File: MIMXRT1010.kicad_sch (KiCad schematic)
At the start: 28 parts, among them J1 Conn_01x02, U1 MIMXRT1011DAE5A, Y1 32.68KHz, Y2 24 MHZ

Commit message: anjir
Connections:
- net LPUART3_RXD_ALT0: now reaches U1.1 (GPIO_11)
- net LPUART4_TXD_ALT0: now reaches U1.58 (GPIO_AD_02)
- net LPUART4_RXD_ALT0: now reaches U1.59 (GPIO_AD_01)
- net LPUART1_TXD_ALT2: now reaches U1.62 (GPIO_SD_12)
- net LPUART1_RXD_ALT2: now reaches U1.64 (GPIO_SD_11)
- net LPUART2_TXD_ALT2: now reaches U1.65 (GPIO_SD_10)
- net LPUART2_RXD_ALT2: now reaches U1.66 (GPIO_SD_09)
- net LPUART3_TXD_ALT0: now reaches U1.80 (GPIO_12)
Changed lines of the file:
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@@
+	(wire
+		(pts
+			(xy 212.09 41.91) (xy 245.11 41.91)
+		)
+		(stroke
+			(width 0)
+			(type default)
+		)
+	)
 	(wire
 		(pts
@@
 	(wire
 		(pts
-			(xy 212.09 133.35) (xy 224.79 133.35)
+			(xy 212.09 133.35) (xy 241.3 133.35)
 		)
 		(stroke
@@
 	(wire
 		(pts
+			(xy 212.09 95.25) (xy 234.95 95.25)
+		)
+		(stroke
+			(width 0)
+			(type default)
+		)
+	)
+	(wire
+		(pts
 			(xy 20.32 118.11) (xy 20.32 129.54)
 		)
@@
 	(wire
 		(pts
+			(xy 212.09 80.01) (xy 237.49 80.01)
+		)
+		(stroke
+			(width 0)
+			(type default)
+		)
+	)
+	(wire
+		(pts
 			(xy 247.65 138.43) (xy 252.73 138.43)
 		)
@@
 	(wire
 		(pts
+			(xy 212.09 77.47) (xy 237.49 77.47)
+		)
+		(stroke
+			(width 0)
+			(type default)
+		)
+	)
+	(wire
+		(pts
 			(xy 99.06 158.75) (xy 99.06 157.48)
 		)
@@
 	(wire
 		(pts
+			(xy 58.42 41.91) (xy 85.09 41.91)
+		)
+		(stroke
+			(width 0)
+			(type default)
+		)
+	)
+	(wire
+		(pts
 			(xy 21.59 78.74) (xy 50.8 78.74)
 		)
@@
 	(wire
 		(pts
+			(xy 212.09 97.79) (xy 234.95 97.79)
+		)
+		(stroke
+			(width 0)
+			(type default)
+		)
+	)
+	(wire
+		(pts
 			(xy 85.09 135.89) (xy 69.85 135.89)
 		)
@@
 	(wire
 		(pts
+			(xy 212.09 87.63) (xy 237.49 87.63)
+		)
+		(stroke
+			(width 0)
+			(type default)
+		)
+	)
+	(wire
+		(pts
 			(xy 16.51 106.68) (xy 16.51 105.41)
 		)
@@
 	(wire
 		(pts
+			(xy 212.09 82.55) (xy 237.49 82.55)
+		)
+		(stroke
+			(width 0)
+			(type default)
+		)
+	)
+	(wire
+		(pts
 			(xy 74.93 115.57) (xy 85.09 115.57)
 		)
@@
 	(wire
 		(pts
-			(xy 212.09 130.81) (xy 224.79 130.81)
+			(xy 212.09 130.81) (xy 241.3 130.81)
 		)
 		(stroke
@@
 			(width 0)
 			(type default)
+		)
+	)
+	(text_box "LPUART3 => GNSS\nLPUART1/2 => WIFI\nLPUART4 => PRINTER (KAYAKNYA)\n\nCOMCONFIGURASI LEWAT APA NJIR?"
+		(exclude_from_sim no)
+		(at 17.78 20.32 0)
+		(size 33.02 17.78)
+		(stroke
+			(width 0)
+			(type default)
+		)
+		(fill
+			(type none)
+		)
+		(effects
+			(font
+				(size 1.27 1.27)
+			)
+			(justify left top)
 		)
 	)
@@
 		)
 	)
+	(label "LPUART4_RXD_ALT0"
+		(at 234.95 95.25 180)
+		(fields_autoplaced yes)
+		(effects
+			(font
+				(size 1.27 1.27)
+			)
+			(justify right bottom)
+		)
+	)
 	(label "LPSPI1_SDI"
 		(at 227.33 100.33 180)
@@
 	)
 	(label "JTAG_TCK"
-		(at 224.79 130.81 180)
+		(at 241.3 130.81 180)
 		(fields_autoplaced yes)
 		(effects
@@
 		)
 	)
+	(label "LPUART3_TXD_ALT0"
+		(at 245.11 41.91 180)
+		(fields_autoplaced yes)
+		(effects
+			(font
+				(size 1.27 1.27)
+			)
+			(justify right bottom)
+		)
+	)
+	(label "LPUART2_RXD_ALT2"
+		(at 237.49 77.47 180)
+		(fields_autoplaced yes)
+		(effects
+			(font
+				(size 1.27 1.27)
+			)
+			(justify right bottom)
+		)
+	)
 	(label "OTG1_DN"
 		(at 73.66 120.65 0)
@@
 		)
 	)
+	(label "LPUART3_RXD_ALT0"
+		(at 58.42 41.91 0)
+		(fields_autoplaced yes)
+		(effects
+			(font
+				(size 1.27 1.27)
+			)
+			(justify left bottom)
+		)
+	)
 	(label "JTAG_TDO"
 		(at 224.79 123.19 180)
@@
 		)
 	)
+	(label "LPUART4_TXD_ALT0"
+		(at 234.95 97.79 180)
+		(fields_autoplaced yes)
+		(effects
+			(font
+				(size 1.27 1.27)
+			)
+			(justify right bottom)
+		)
+	)
 	(label "JTAG_TMS"
-		(at 224.79 133.35 180)
-		(fields_autoplaced yes)
-		(effects
+		(at 241.3 133.35 180)
+		(fields_autoplaced yes)
+		(effects
+			(font
+				(size 1.27 1.27)
+			)
+			(justify right bottom)
+		)
+	)
+	(label "LPUART1_TXD_ALT2"
+		(at 237.49 87.63 180)
+		(fields_autoplaced yes)
+		(effects
+			(font
+				(size 1.27 1.27)
+			)
+			(justify right bottom)
+		)
+	)
+	(label "LPUART2_TXD_ALT2"
+		(at 237.49 80.01 180)
+		(fields_autoplaced yes)
+		(effects
+			(font
+				(size 1.27 1.27)
+			)
+			(justify right bottom)
+		)
+	)
+	(label "LPUART1_RXD_ALT2"
+		(at 237.49 82.55 180)
+		(fields_autoplaced yes)
+		(effects

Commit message: yara me kya karun
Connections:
- net GPIO_03_ALT2: now reaches U1.10 (GPIO_03)
- net C1_KEYPAD: now reaches U1.67 (GPIO_SD_08)
- net C2_KEYPAD: now reaches U1.68 (GPIO_SD_07)
- net C3_KEYPAD: now reaches U1.69 (GPIO_SD_06)
- net C4_KEYPAD: now reaches U1.70 (GPIO_SD_05)
- net R1_KEYPAD: now reaches U1.72 (GPIO_SD_04)
- net R2_KEYPAD: now reaches U1.73 (GPIO_SD_03)
- net R3_KEYPAD: now reaches U1.74 (GPIO_SD_02)
- net R4_KEYPAD: now reaches U1.75 (GPIO_SD_01)
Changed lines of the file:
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@@
+	(wire
+		(pts
+			(xy 212.09 74.93) (xy 218.44 74.93)
+		)
+		(stroke
+			(width 0)
+			(type default)
+		)
+	)
 	(wire
 		(pts
@@
 	(wire
 		(pts
+			(xy 212.09 62.23) (xy 220.98 62.23)
+		)
+		(stroke
+			(width 0)
+			(type default)
+		)
+	)
+	(wire
+		(pts
 			(xy 224.79 151.13) (xy 236.22 151.13)
 		)
@@
 	(wire
 		(pts
+			(xy 212.09 59.69) (xy 220.98 59.69)
+		)
+		(stroke
+			(width 0)
+			(type default)
+		)
+	)
+	(wire
+		(pts
 			(xy 48.26 158.75) (xy 48.26 160.02)
 		)
@@
 	(wire
 		(pts
+			(xy 212.09 57.15) (xy 220.98 57.15)
+		)
+		(stroke
+			(width 0)
+			(type default)
+		)
+	)
+	(wire
+		(pts
 			(xy 85.09 135.89) (xy 69.85 135.89)
 		)
@@
 	(wire
 		(pts
+			(xy 212.09 67.31) (xy 218.44 67.31)
+		)
+		(stroke
+			(width 0)
+			(type default)
+		)
+	)
+	(wire
+		(pts
 			(xy 16.51 114.3) (xy 16.51 115.57)
 		)
@@
 	(wire
 		(pts
+			(xy 212.09 72.39) (xy 218.44 72.39)
+		)
+		(stroke
+			(width 0)
+			(type default)
+		)
+	)
+	(wire
+		(pts
 			(xy 212.09 102.87) (xy 227.33 102.87)
 		)
@@
 	(wire
 		(pts
+			(xy 49.53 64.77) (xy 85.09 64.77)
+		)
+		(stroke
+			(width 0)
+			(type default)
+		)
+	)
+	(wire
+		(pts
 			(xy 224.79 148.59) (xy 224.79 151.13)
 		)
@@
 	(wire
 		(pts
+			(xy 212.09 54.61) (xy 220.98 54.61)
+		)
+		(stroke
+			(width 0)
+			(type default)
+		)
+	)
+	(wire
+		(pts
 			(xy 48.26 110.49) (xy 48.26 114.3)
+		)
+		(stroke
+			(width 0)
+			(type default)
+		)
+	)
+	(wire
+		(pts
+			(xy 212.09 69.85) (xy 218.44 69.85)
 		)
 		(stroke
@@
 		)
 	)
+	(label "MCU_PWM_CERVO"
+		(at 49.53 64.77 180)
+		(fields_autoplaced yes)
+		(effects
+			(font
+				(size 1.27 1.27)
+			)
+			(justify right bottom)
+		)
+	)
+	(label "C2_KEYPAD"
+		(at 218.44 72.39 0)
+		(fields_autoplaced yes)
+		(effects
+			(font
+				(size 1.27 1.27)
+			)
+			(justify left bottom)
+		)
+	)
+	(label "C1_KEYPAD"
+		(at 218.44 74.93 0)
+		(fields_autoplaced yes)
+		(effects
+			(font
+				(size 1.27 1.27)
+			)
+			(justify left bottom)
+		)
+	)
 	(label "LPSPI1_SCK"
 		(at 227.33 113.03 180)
@@
 		)
 	)
+	(label "C4_KEYPAD"
+		(at 218.44 67.31 0)
+		(fields_autoplaced yes)
+		(effects
+			(font
+				(size 1.27 1.27)
+			)
+			(justify left bottom)
+		)
+	)
 	(label "LPUART4_RXD_ALT0"
 		(at 234.95 95.25 180)
@@
 		)
 	)
+	(label "GPIO_03_ALT2"
+		(at 58.42 64.77 0)
+		(fields_autoplaced yes)
+		(effects
+			(font
+				(size 1.27 1.27)
+			)
+			(justify left bottom)
+		)
+	)
 	(label "5V_USB_OTG"
 		(at 21.59 78.74 0)
@@
 		)
 	)
+	(label "R1_KEYPAD"
+		(at 220.98 62.23 0)
+		(fields_autoplaced yes)
+		(effects
+			(font
+				(size 1.27 1.27)
+			)
+			(justify left bottom)
+		)
+	)
 	(label "DCDC_3V3"
 		(at 262.89 52.07 0)
@@
 		)
 	)
+	(label "C3_KEYPAD"
+		(at 218.44 69.85 0)
+		(fields_autoplaced yes)
+		(effects
+			(font
+				(size 1.27 1.27)
+			)
+			(justify left bottom)
+		)
+	)
 	(label "OTG1_DP"
 		(at 73.66 123.19 0)
@@
 		)
 	)
+	(label "R3_KEYPAD"
+		(at 220.98 57.15 0)
+		(fields_autoplaced yes)
+		(effects
+			(font
+				(size 1.27 1.27)
+			)
+			(justify left bottom)
+		)
+	)
 	(label "LPUART3_TXD_ALT0"
 		(at 245.11 41.91 180)
@@
 		)
 	)
+	(label "R2_KEYPAD"
+		(at 220.98 59.69 0)
+		(fields_autoplaced yes)
+		(effects
+			(font
+				(size 1.27 1.27)
+			)
+			(justify left bottom)
+		)
+	)
 	(label "JTAG_TMS"
 		(at 241.3 133.35 180)
@@
 		)
 	)
+	(label "R4_KEYPAD"
+		(at 220.98 54.61 0)
+		(fields_autoplaced yes)
+		(effects
+			(font
+				(size 1.27 1.27)
+			)
+			(justify left bottom)
+		)
+	)

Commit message: sebelum pemeriksaan terkahir
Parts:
- removed C18: 1.0UF, symbol Device:C_Polarized_US
- removed C19: 0.22UF, symbol Device:C_Polarized_US
- removed J1: Conn_01x02, symbol Connector_Generic:Conn_01x02
- removed R6: DNP, symbol Device:R_US
- added L5: 4.7uH, symbol Device:L
- added R58: 0, symbol Device:R_US
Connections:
- net C1_KEYPAD: now also U1.46 (GPIO_AD_11); no longer U1.67 (GPIO_SD_08)
- net C2_KEYPAD: now also U1.11 (GPIO_02); no longer U1.68 (GPIO_SD_07)
- net C3_KEYPAD: now also U1.12 (GPIO_01); no longer U1.69 (GPIO_SD_06)
- net C4_KEYPAD: now also U1.60 (GPIO_AD_00); no longer U1.70 (GPIO_SD_05)
- net GND: now also U1.34 (NGND_KEL0), R58.1
- net R3_KEYPAD: now also U1.9 (GPIO_04); no longer U1.74 (GPIO_SD_02)
- net R4_KEYPAD: now also U1.79 (GPIO_13); no longer U1.75 (GPIO_SD_01)
- net VDDA_ADC_3P3_MCU: now reaches U1.42
- net GPIO_00: now reaches U1.13 (GPIO_00)
- net VDD_SOC_IN: now reaches U1.14
- net VDD_SOC_IN: now also U1.53 (VDD_SOC_IN), U1.77 (VDD_SOC_IN)
- net DCDC_PSWITCH_MCU: now reaches U1.15 (DCDC_PSWITCH)
- net MCU_DCDC_IN: now reaches U1.17 (DCDC_IN_Q)
- net MCU_DCDC_IN: now also U1.18 (DCDC_IN)
- net at U1.19 (DCDC_LP): now also L5.2
- net LPI2C2_SCL: now reaches U1.2 (GPIO_10)
- net ONOFF: now reaches U1.21 (ONOFF)
- net POR_B: now reaches U1.22 (POR_B)
- net at U1.23 (TEST_MODE): now also R58.2
- net PMIC_ON_REQ: now reaches U1.24 (PMIC_ON_REQ)
- net VDD_SNVS_IN: now reaches U1.25 (VDD_SNVS_IN)
- net LPI2C2_SDA: now reaches U1.3 (GPIO_09)
- net VDDA_2P5_CAP: now reaches U1.35 (VDD_HIGH_CAP)
- net VDD_HIGH_IN_MCU: now reaches U1.39 (VDD_HIGH_IN)
- net buzzer: now reaches U1.4 (GPIO_08)
- net VDDA_1P1_CAP: now reaches C16.1, C17.1, U1.40 (NVCC_PLL)
- net GREEN_LED: now reaches U1.5 (GPIO_07)
- net BLUE_LED: now reaches U1.6 (GPIO_06)
- net alrt: now reaches U1.76 (GPIO_SD_00)
- net RED_LED: now reaches U1.8 (GPIO_05)
- net LPUART1_TXD_ALT2 renamed FlexSPI_D3_A
- net LPUART2_RXD_ALT2 renamed FlexSPI_D0_A
- net LPUART2_TXD_ALT2 renamed FlexSPI_CLK_A
- new net DCDC_OUT: L5.1
- new net FlexSPI_D1_A: U1.68 (GPIO_SD_07)
- new net FlexSPI_D2_A: U1.67 (GPIO_SD_08)
- new net FlexSPI_SS0: U1.69 (GPIO_SD_06)
- new net LPI2C1_SCL: U1.74 (GPIO_SD_02)
- new net LPI2C1_SDA: U1.75 (GPIO_SD_01)
- new net USER_BUTTON: U1.70 (GPIO_SD_05)

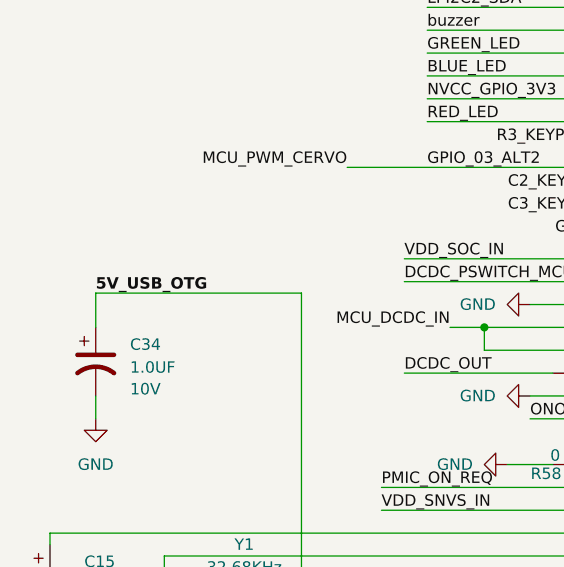
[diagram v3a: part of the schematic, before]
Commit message: Add power usb
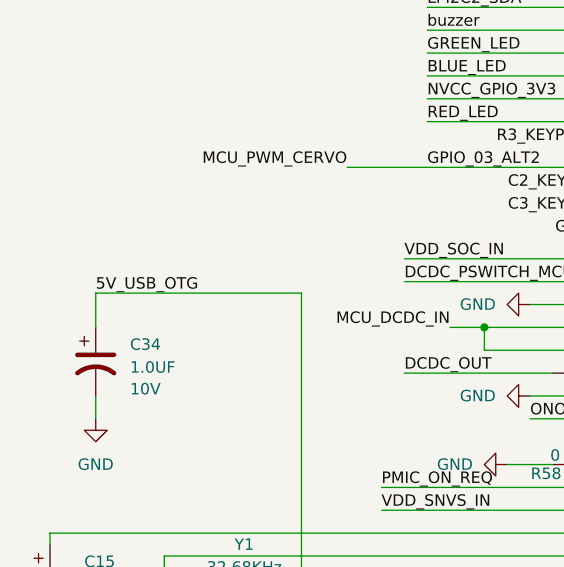
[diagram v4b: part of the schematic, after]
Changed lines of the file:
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@@
 			(font
 				(size 1.27 1.27)
-				(bold yes)
 			)
 			(justify left bottom)

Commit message: adad
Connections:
- net ADD_EL3: now reaches U1.43 (GPIO_AD_14)
- net ADD_EL2: now reaches U1.51 (GPIO_AD_07)
- net ADD_EL1: now reaches U1.61 (GPIO_SD_13)
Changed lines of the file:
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@@
+	(wire
+		(pts
+			(xy 212.09 90.17) (xy 214.63 90.17)
+		)
+		(stroke
+			(width 0)
+			(type default)
+		)
+	)
 	(wire
 		(pts
@@
 	(wire
 		(pts
+			(xy 212.09 135.89) (xy 231.14 135.89)
+		)
+		(stroke
+			(width 0)
+			(type default)
+		)
+	)
+	(wire
+		(pts
 			(xy 63.5 149.86) (xy 69.85 149.86)
 		)
@@
 		(pts
 			(xy 85.09 140.97) (xy 85.09 148.59)
+		)
+		(stroke
+			(width 0)
+			(type default)
+		)
+	)
+	(wire
+		(pts
+			(xy 212.09 115.57) (xy 222.25 115.57)
 		)
 		(stroke
@@
 		(fields_autoplaced yes)
 		(effects
+			(font
+				(size 1.27 1.27)
+			)
+			(justify left bottom)
+		)
+	)
+	(label "ADD_EL1"
+		(at 214.63 90.17 0)
+		(fields_autoplaced yes)
+		(effects
+			(font
+				(size 1.27 1.27)
+			)
+			(justify left bottom)
+		)
+	)
+	(label "ADD_EL2"
+		(at 222.25 115.57 0)
+		(fields_autoplaced yes)
+		(effects
+			(font
+				(size 1.27 1.27)
+			)
+			(justify left bottom)
+		)
+	)
+	(label "ADD_EL3"
+		(at 231.14 135.89 0)
+		(fields_autoplaced yes)
+		(effects

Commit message: menambah lebih dari setengah footprint
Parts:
- C1, C2: value 10 pf -> 10 PF; footprint (none) -> Capacitor_SMD:C_0402_1005Metric
- C10, C11, C12, C13, C14, C21, C8, C9: footprint (none) -> Capacitor_SMD:C_0402_1005Metric; MANUFACTURER (none) -> CC0402KRX5R6BB104
- C15: footprint (none) -> Capacitor_SMD:C_0402_1005Metric; MANUFACTURER (none) -> CL10A226MQ8NRNE
- C16: value 0.22uF -> 0.22UF; footprint (none) -> Capacitor_SMD:C_0402_1005Metric; MANUFACTURER (none) -> CL10A226MQ8NRNE
- C17: value 4.7uF -> 4.7UF; footprint (none) -> Capacitor_SMD:C_0402_1005Metric; MANUFACTURER (none) -> C1005X5R0J475M050BC
- C20: value 10uf -> 10UF; footprint (none) -> Capacitor_SMD:C_0603_1608Metric; MANUFACTURER (none) -> GRM188R61A106KE69D
- C3, C4: value 4.7pF -> 4.7PF; footprint (none) -> Capacitor_SMD:C_0402_1005Metric
- C34: value 1.0UF -> 1UF; footprint (none) -> Capacitor_SMD:C_0402_1005Metric
- R2, R5, R58: footprint (none) -> Resistor_SMD:R_0402_1005Metric
- U1: footprint MIMXRT1011DAE5A_NXP -> footprints:MIMXRT1011DAE5A_NXP

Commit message: menambahkan beberapa component lagi
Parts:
- L5: footprint (none) -> Capacitor_SMD:C_0402_1005Metric
- TP1: footprint (none) -> MountingHole:MountingHole_2.1mm
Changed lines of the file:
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@@
 			)
 		)
-		(property "Footprint" ""
+		(property "Footprint" "MountingHole:MountingHole_2.1mm"
 			(at 57.15 125.73 0)
 			(effects
@@
 			)
 		)
-		(property "Footprint" ""
+		(property "Footprint" "Capacitor_SMD:C_0402_1005Metric"
 			(at 76.2 87.63 0)
 			(effects
